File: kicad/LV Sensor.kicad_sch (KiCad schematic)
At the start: 12 parts, among them U1 MCP2518FD-xJHA, U2 74LVC1G3157GW_125, U3 XMSM0C1104SPW20R, U4 ADS8689TSSOP, U5 TLV77312PDBVR, U6 AS358MTR-G1

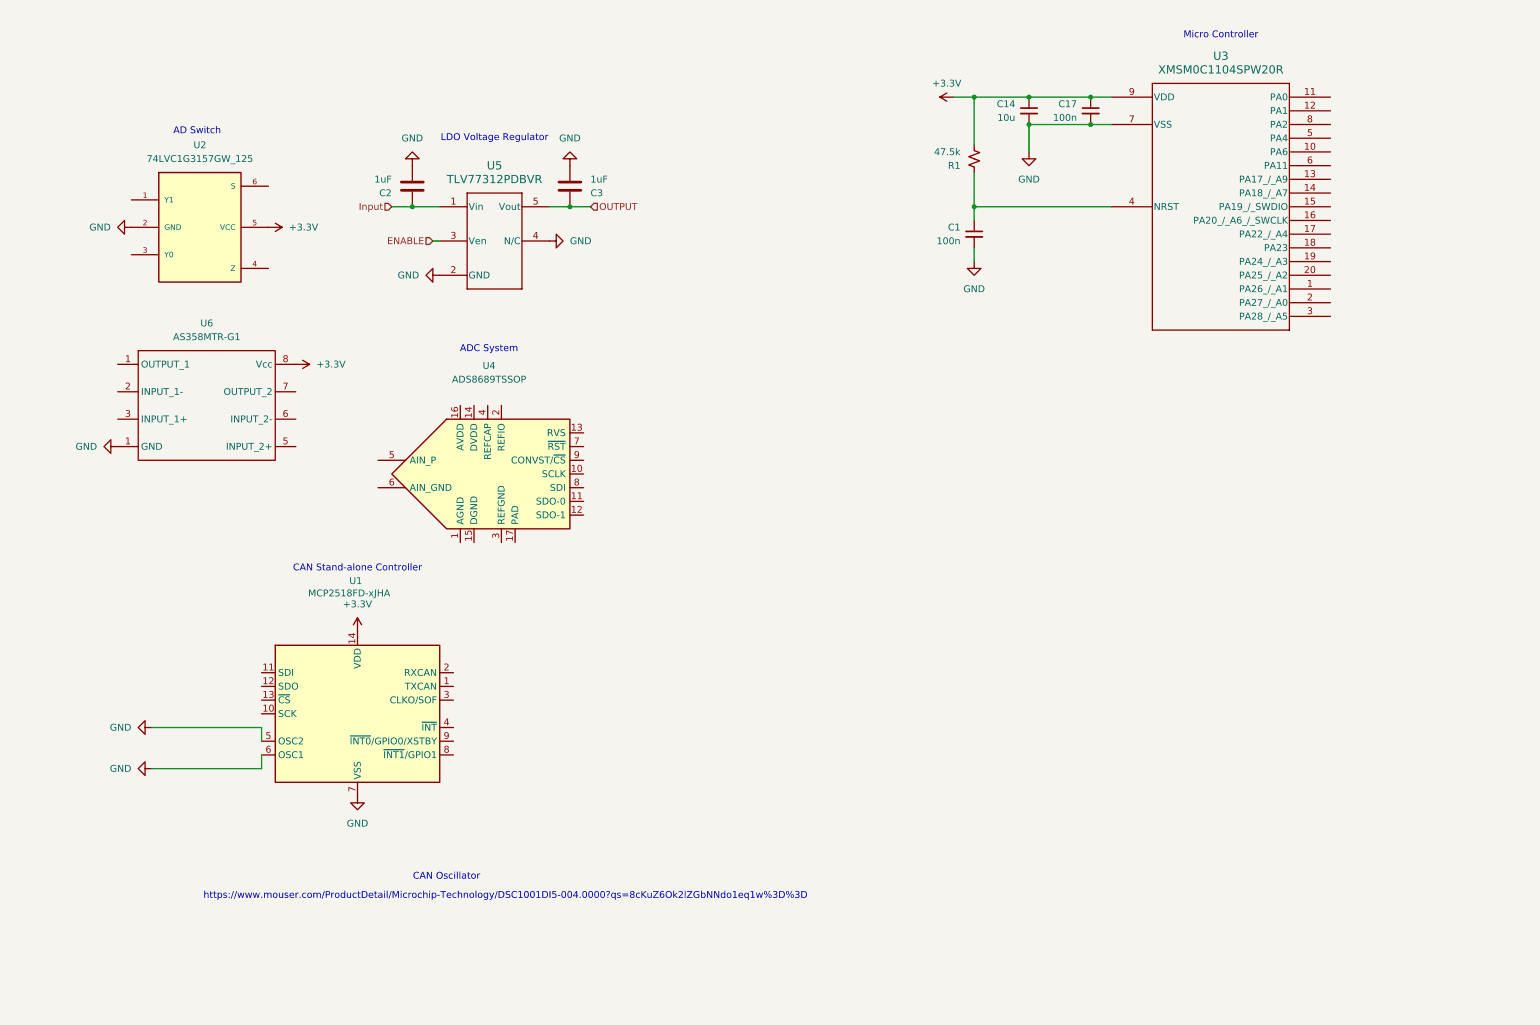
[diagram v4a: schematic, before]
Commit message: 08-28-25 Changed symbols to match new components
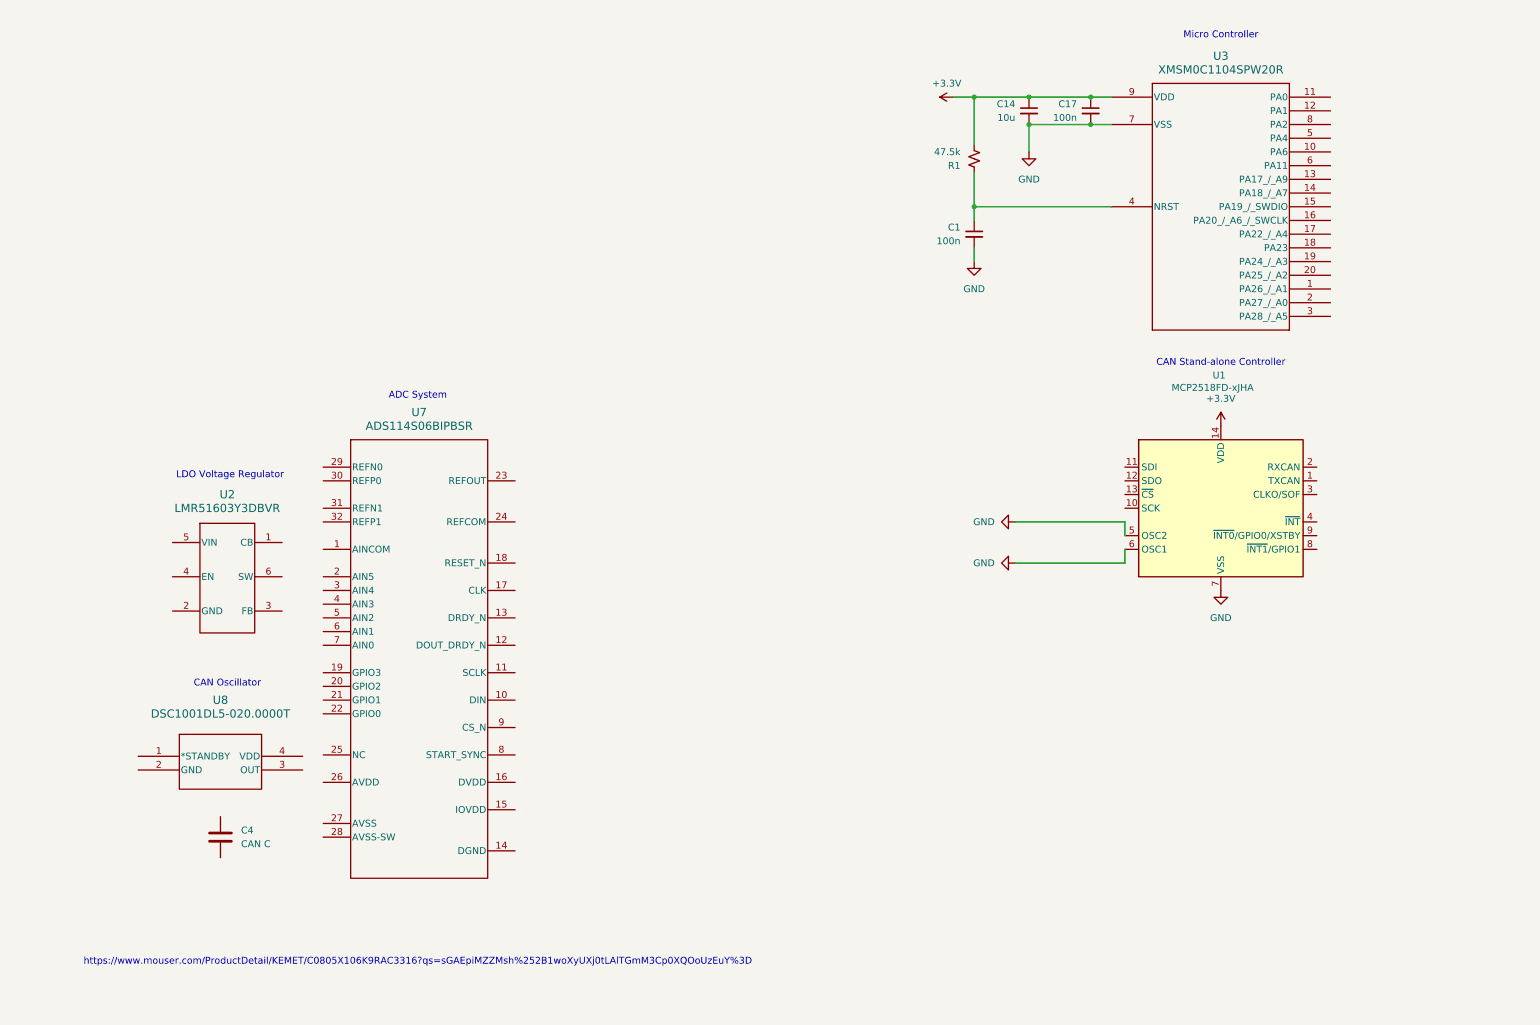
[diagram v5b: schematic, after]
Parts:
- removed C2, C3: 1uF, symbol Device:C
- removed U2: 74LVC1G3157GW_125, LV Sensor:74LVC1G3157GW_SOT363-2, symbol 74LVC1G3157GW_125:74LVC1G3157GW_125
- removed U4: ADS8689TSSOP, Package_DFN_QFN:QFN-16-1EP_4x4mm_P0.65mm_EP2.7x2.7mm, symbol LV-Sensor-Lib:ADS8689TSSOP
- removed U5: TLV77312PDBVR, DBV0005A-IPC_A, symbol TLV77333PDBVR:TLV77312PDBVR
- removed U6: AS358MTR-G1, symbol LV-Sensor-Lib:AS358MTR-G1
- added C4: CAN C, symbol Device:C
- added U2: LMR51603Y3DBVR, DBV0006A-MFG-IPC_A, symbol LV-Sensor-Lib:LMR51603Y3DBVR
- added U7: ADS114S06BIPBSR, PBS0032A_N, symbol LV-Sensor-Lib:ADS114S06BIPBSR
- added U8: DSC1001DL5-020.0000T, CDFN4_2P5X2_MCH, symbol LV-Sensor-Lib:DSC1001DL5-020.0000T
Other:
- note added: "https://www.mouser.com/ProductDetail/KEMET/C0805X106K9RAC3316?qs=sGAEpiMZZMsh%252B1woXyUXj0tLAlTGmM3Cp0XQOoUzEuY%3D"
- note removed: "AD Switch"
- note removed: "https://www.mouser.com/ProductDetail/Microchip-Technology/DSC1001DI5-004.0000?qs=8cKuZ6Ok2lZGbNNdo1eq1w%3D%3D"
- moved on the sheet: U1

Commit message: Added buck converter to schematic and set it up for use
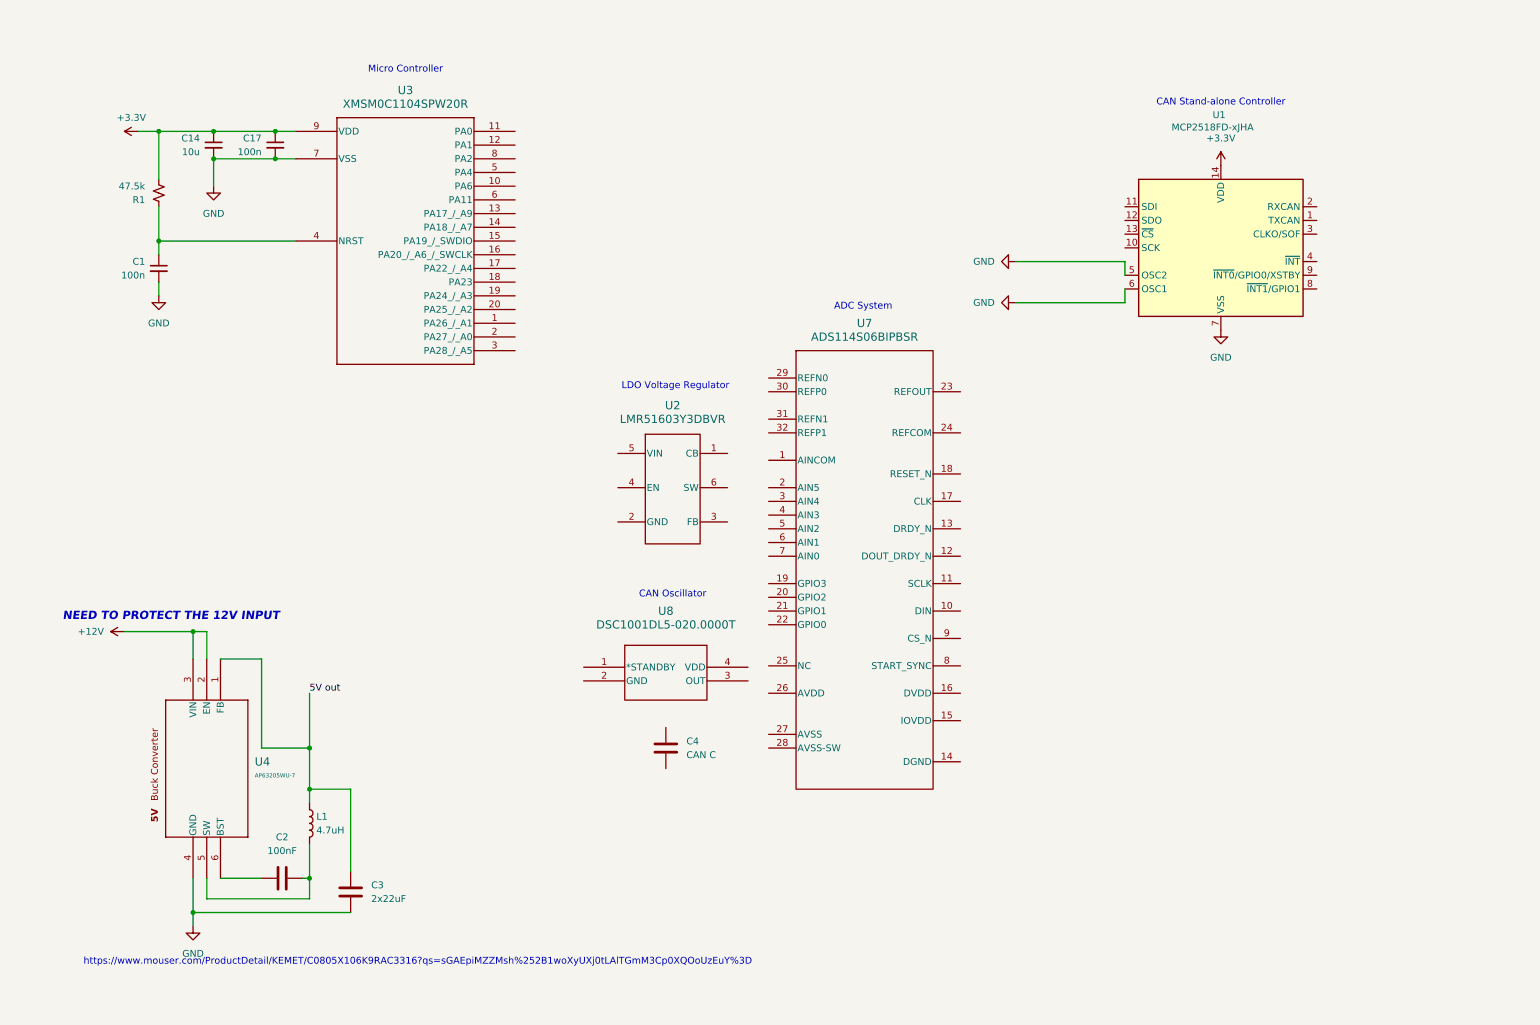
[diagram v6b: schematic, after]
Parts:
- added C2: 100nF, symbol Device:C
- added C3: 2x22uF, symbol Device:C
- added L1: 4.7uH, symbol Device:L
- added U4: AP63205WU-7, SOIC_05WU-7_DIO, symbol LV-Sensor-Lib:AP63205WU-7
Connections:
- net GND: now also C3.1, U4.4 (GND)
- new net: C2.1, U4.6 (BST)
- new net: C2.2, L1.2, U4.5 (SW)
- new net +12V: U4.2 (EN), U4.3 (VIN)
- new net 5V out: C3.2, L1.1, U4.1 (FB)
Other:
- note added: "NEED TO PROTECT THE 12V INPUT"
- moved on the sheet: C1, C14, C17, C4, R1, U1, U2, U3, U7, U8

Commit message: Mostly setup CAN, hooked it up to the MCU, and chose the I/O pins to be used on the MCU.
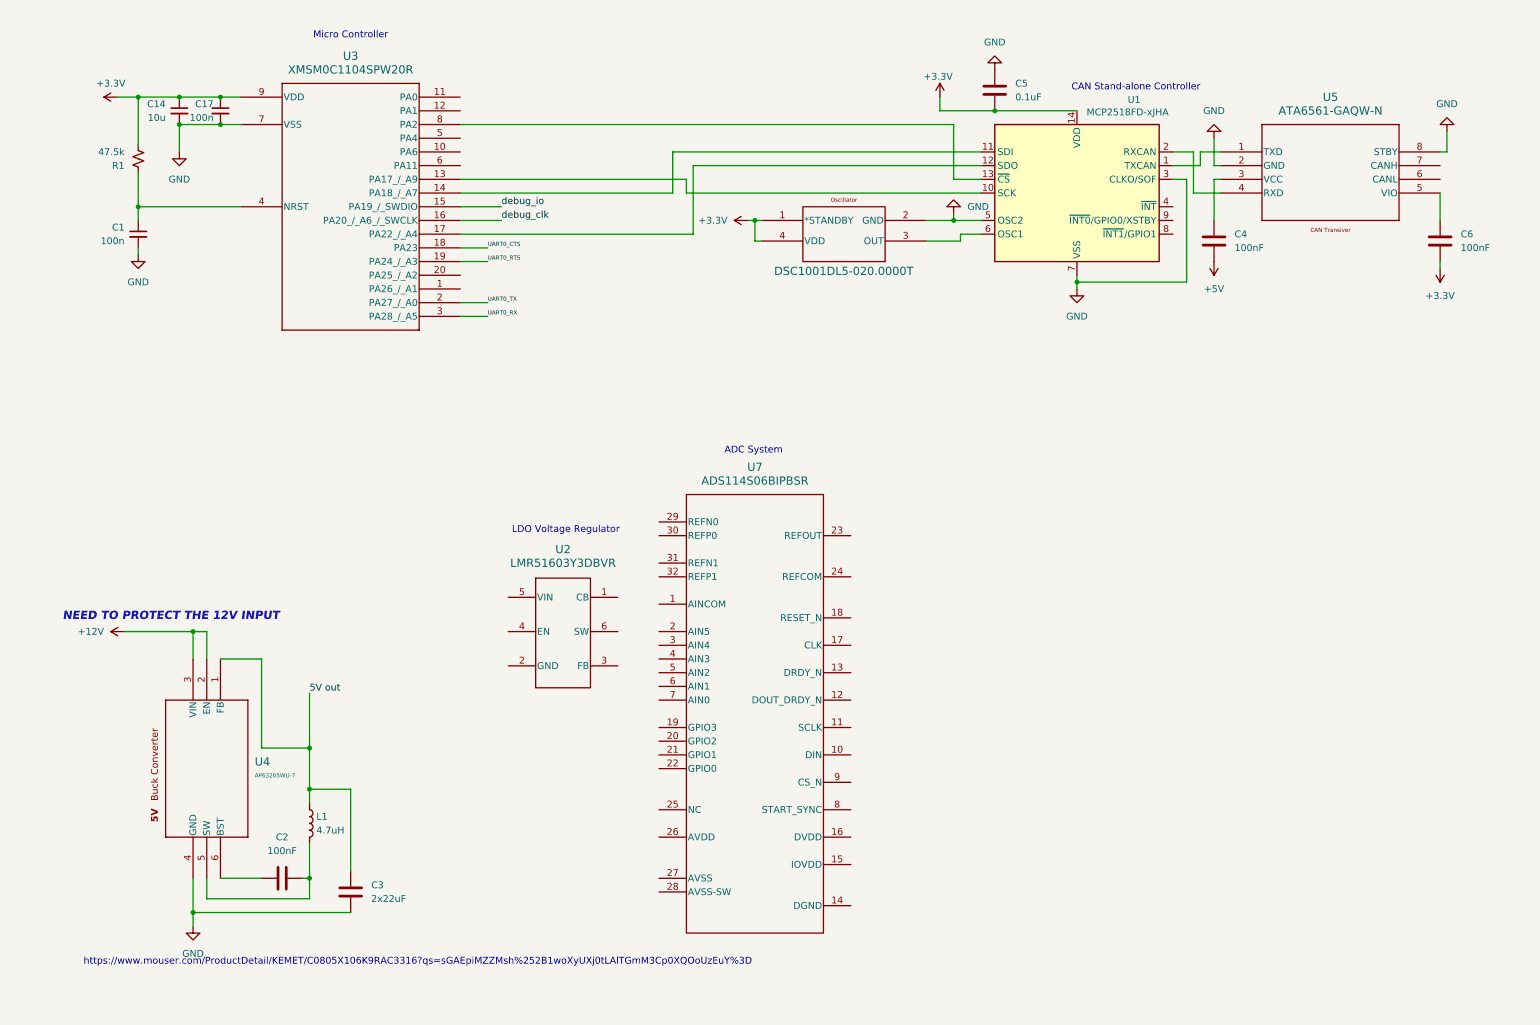
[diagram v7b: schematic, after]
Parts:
- removed U8: DSC1001DL5-020.0000T, CDFN4_2P5X2_MCH, symbol LV-Sensor-Lib:DSC1001DL5-020.0000T
- added C5: 0.1uF, symbol Device:C
- added C6: 100nF, symbol Device:C
- added U5: ATA6561-GAQW-N, SOIC8_4P9X3P9MC_MCH, symbol LV-Sensor-Lib:ATA6561-GAQW-N
- added U6: DSC1001DL5-020.0000T, CDFN4_2P5X2_MCH, symbol LV-Sensor-Lib:DSC1001DL5-020.0000T
- C4: value CAN C -> 100nF; mouser https://www.mouser.com/ProductDetail/KYOCERA-AVX/06033A400K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 -> (none); specs 40 pF, 25 VDC, 10%, -55 to + 125 C -> (none); unit x10 0.149 -> (none)
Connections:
- net +3.3V: now also C5.2, C6.2, U6.1 (*STANDBY), U6.4 (VDD)
- net GND: now also U1.3 (CLKO/SOF), C5.1, U5.2 (GND), U5.8 (STBY), U6.2 (GND); no longer U1.6 (OSC1)
- net at U3.13 (PA17_/_A9): now also U1.10 (SCK)
- net at U3.14 (PA18_/_A7): now also U1.11 (SDI)
- net debug_io: now reaches U3.15 (PA19_/_SWDIO)
- net debug_clk: now reaches U3.16 (PA20_/_A6_/_SWCLK)
- net at U3.17 (PA22_/_A4): now also U1.12 (SDO)
- net UART0_CTS: now reaches U3.18 (PA23)
- net UART0_RTS: now reaches U3.19 (PA24_/_A3)
- net UART0_TX: now reaches U3.2 (PA27_/_A0)
- net UART0_RX: now reaches U3.3 (PA28_/_A5)
- net at U3.8 (PA2): now also U1.13 (~{CS})
- net at U1.1 (TXCAN): now also U5.1 (TXD)
- net at U1.2 (RXCAN): now also U5.4 (RXD)
- net at C4.1: now also U5.3 (VCC)
- net +5V: now reaches C4.2
- new net: C6.1, U5.5 (VIO)
- new net: U1.6 (OSC1), U6.3 (OUT)
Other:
- note removed: "CAN Oscillator"
- moved on the sheet: C1, C14, C17, R1, U1, U2, U3, U7

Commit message: Completed the voltage inverter; still needs to be hooked up to ADC and a 2.5V reference made for it.
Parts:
- added C10, C9: 47uF, symbol Device:C_Small
- added C7: 0.01uF, symbol Device:C_Small
- added C8: 15pF, symbol Device:C_Small
- added U8: LM2662MX/NOPB, M08A, symbol LV-Sensor-Lib:LM2662MX_NOPB
- U6: value DSC1001DL5-020.0000T -> DSC1001DL5
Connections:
- net +3.3V: now also C7.1
- net GND: now also C10.2, C8.1, U8.3 (GND), U8.6 (LV)
- net at U3.13 (PA17_/_A9): no longer U1.10 (SCK)
- net at U3.14 (PA18_/_A7): no longer U1.11 (SDI)
- net at U3.17 (PA22_/_A4): no longer U1.12 (SDO)
- net at U1.6 (OSC1), U6.3 (OUT): now also C7.2, C8.2
- new net: C9.1, U8.2 (C1+)
- new net: C9.2, U8.4 (C1-)
- new net: C10.1, U8.5 (OUT)
- new net +2V5: U8.1 (FC), U8.8 (V+)
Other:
- note added: "SCLK"
- note added: "SDI"
- note added: "SDO"
- note removed: "LDO Voltage Regulator"
- note removed: "https://www.mouser.com/ProductDetail/KEMET/C0805X106K9RAC3316?qs=sGAEpiMZZMsh%252B1woXyUXj0tLAlTGmM3Cp0XQOoUzEuY%3D"
- moved on the sheet: U2, U7
